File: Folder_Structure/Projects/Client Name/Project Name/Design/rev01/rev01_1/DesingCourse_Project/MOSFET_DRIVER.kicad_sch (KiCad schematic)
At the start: 42 parts, among them U2 DRV8302DCA

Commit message: Update 6
SCH and LIB for MOSFET page done, missing passive components
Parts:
- removed L1: 22u, symbol Device:L
- added L?: 22u, IND_BOURNS_SDR0805, symbol SDR0805-220ML:SDR0805-220ML
- D4: MPN (none) -> PMEG6020AELR; Manufactuere (none) -> Nexperia
- D5: MPN (none) -> BAT60A; Manufacturer (none) -> Inineon
- U2: MPN (none) -> DRV8302DCA; Manufacturer (none) -> Texas Instruments
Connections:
- net P5V_DRV: now also L?.2
- net PH: now also L?.1
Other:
- note added: "MOSFET DRIVER"
- note removed: "MOSFER DRIVER"
- company: (none) -> Integro Consulting AB
- title: (none) -> PCB Mastery Project

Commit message: Update 11
SCH finishe, missing the labels and logos and adding all passive components
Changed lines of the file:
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@@
 	(text "MOSFET DRIVER\n"
 		(exclude_from_sim no)
-		(at 144.78 20.066 0)
+		(at 160.02 20.32 0)
 		(effects
 			(font

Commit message: Update 12
Until STEP-DOWN page, all components have complete libraries.

Creation and incluison of all logos and labels libraries
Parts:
- removed C22, C23, C24, C25, C26, C27: 1u, symbol Device:C
- removed R18, R20, R22: 39k, symbol Device:R
- added C36, C37, C38, C40, C41, C43: 1u, Capacitor_SMD:C_0603_1608Metric, symbol Device:C
- added R27, R29, R31: 39k, Resistor_SMD:R_0603_1608Metric, symbol Device:R
- C35: value 1u -> 100n
- gave numbers to parts that had none: 1
- renumbered C33 to C24, C31 to C25, C29 to C26, C34 to C27, C32 to C28, C30 to C29, C28 to C30, C21 to C31, C18 to C32, C19 to C33, C20 to C34, C36 to C39, C37 to C42, C38 to C44, C39 to C45, C40 to C46, C41 to C47, D4 to D13, D5 to D14, R12 to R20, R13 to R21, R14 to R22, R11 to R23, R15 to R24, R16 to R25, R17 to R26, R23 to R28, R21 to R30, R19 to R32, U2 to U4
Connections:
- net +VDC: now also C36.1, C37.1, C38.1, C40.1, C41.1, C43.1
- net GND: now also C36.2, C37.2, C38.2, C40.2, C41.2, C43.2
- net H1_VS: now also R31.1
- net H2_VS: now also R29.1
- net H3_VS: now also R27.1
- net SENS1: now also R31.2
- net SENS2: now also R29.2
- net SENS3: now also R27.2

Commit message: Update13
Still working on FP for the MCU
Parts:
- C32, C33, C34, C35, C45, C46, C47: footprint (none) -> Capacitor_SMD:C_0603_1608Metric; Package (none) -> 0603; Temp Coeff (none) -> X7R; Tolerance (none) -> 10%; Voltage Rating (none) -> 10V
- C39, C42, C44: footprint (none) -> Capacitor_SMD:C_0603_1608Metric; Package (none) -> 0603; Temp Coeff (none) -> X5R; Tolerance (none) -> 10%; Voltage Rating (none) -> 10V
- R28, R30, R32: footprint (none) -> Resistor_SMD:R_0603_1608Metric; Package (none) -> 0603; Power Rating (none) -> 1/10W; Tolerance (none) -> 1%

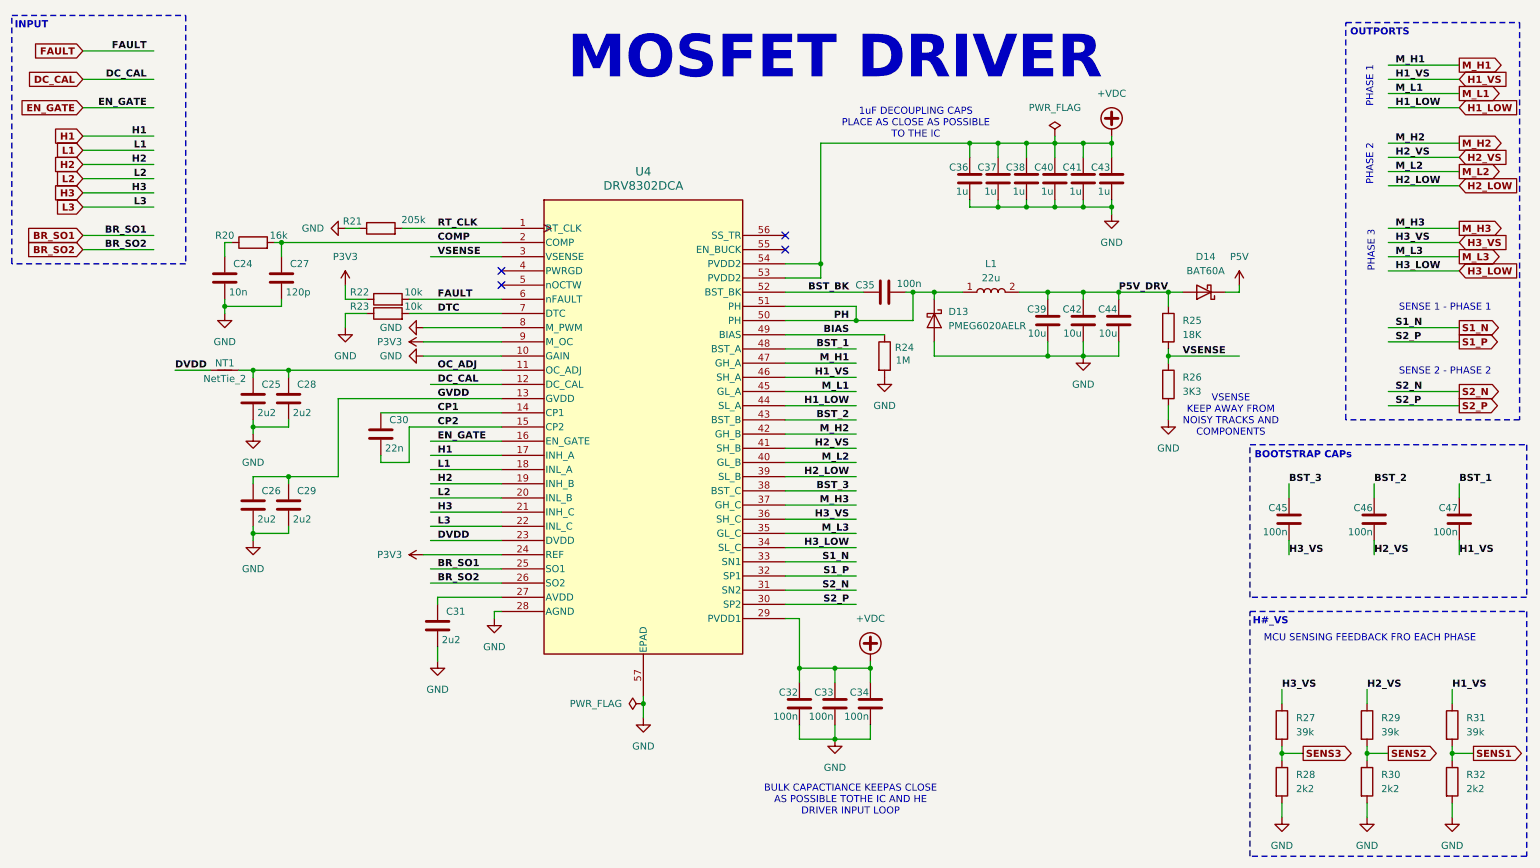
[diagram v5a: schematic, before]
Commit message: Update14
All components with FP, missing the block diagram
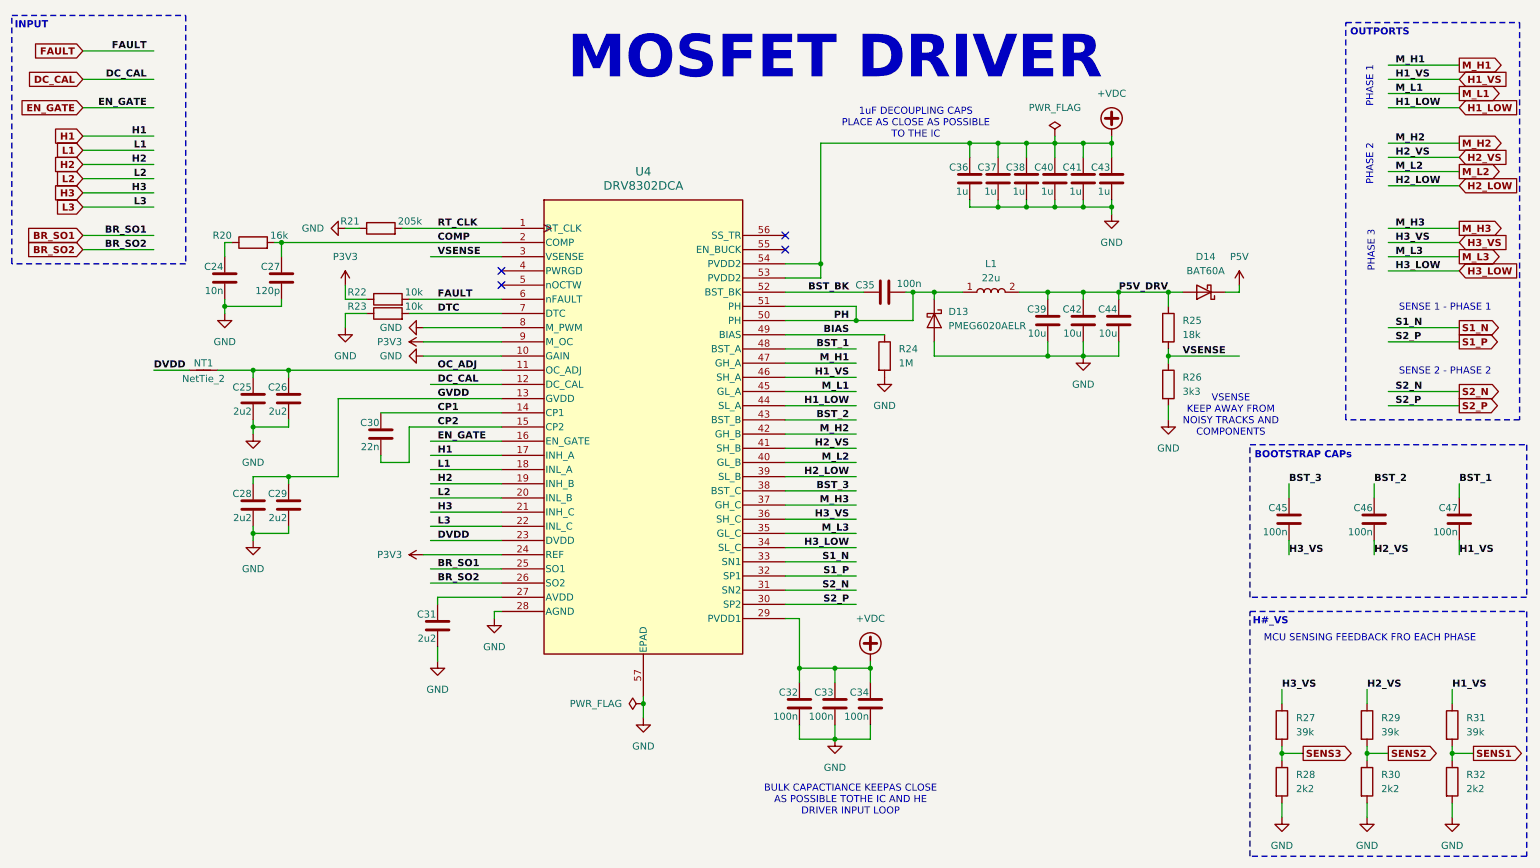
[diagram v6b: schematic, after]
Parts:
- C24, C27: footprint (none) -> Capacitor_SMD:C_0603_1608Metric; Package (none) -> 0603; Temp Coeff (none) -> X7R; Tolerance (none) -> 10%; Voltage Rating (none) -> 50V
- C25, C26, C28, C29, C31: footprint (none) -> Capacitor_SMD:C_0603_1608Metric; Package (none) -> 0603; Temp Coeff (none) -> X5R; Tolerance (none) -> 10%; Voltage Rating (none) -> 6.3V
- C30: footprint (none) -> Capacitor_SMD:C_0603_1608Metric; Package (none) -> 0603; Temp Coeff (none) -> X7R; Tolerance (none) -> 10%; Voltage Rating (none) -> 100V
- D13: Manufactuere Nexperia -> (none); Manufacturer (none) -> Nexperia; Package (none) -> SOD-123
- D14: Manufacturer Inineon -> Infineon; Package (none) -> SOD-323
- NT1: footprint (none) -> NetTie:NetTie-2_SMD_Pad0.5mm
- R20, R21, R22, R23, R24: footprint (none) -> Resistor_SMD:R_0603_1608Metric; Package (none) -> 0603; Power Rating (none) -> 1/10W; Tolerance (none) -> 1%
- R25: value 18K -> 18k; footprint (none) -> Resistor_SMD:R_0603_1608Metric; Package (none) -> 0603; Power Rating (none) -> 1/10W; Tolerance (none) -> 1%
- R26: value 3K3 -> 3k3; footprint (none) -> Resistor_SMD:R_0603_1608Metric; Package (none) -> 0603; Power Rating (none) -> 1/10W; Tolerance (none) -> 1%
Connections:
- net GVDD: now also C28.1; no longer C26.1
- net OC_ADJ: now also C26.1; no longer C28.1
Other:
- moved on the sheet: NT1

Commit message: Update 16
Initial component placement done
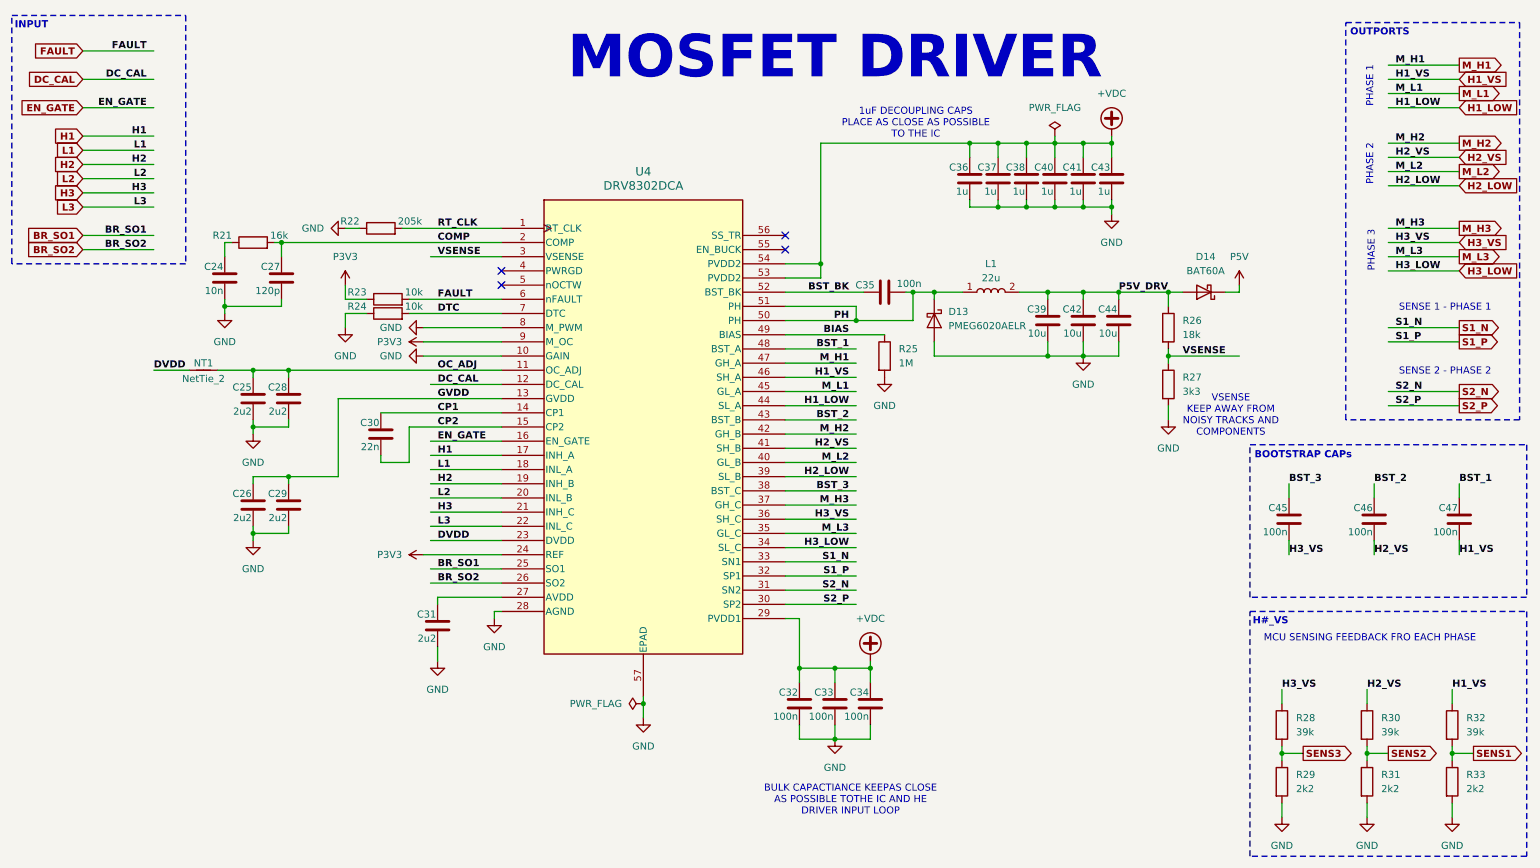
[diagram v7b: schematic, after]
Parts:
- L1: footprint IND_BOURNS_SDR0805 -> L_Bourns_SDR0805:IND_BOURNS_SDR0805
- U4: footprint DCA56_6P35X3P61 -> DRV8302DCA:SOP50P810X120-57N; Package (none) -> 56pin-HTSSOP
- renumbered C28 to C26, C26 to C28, R20 to R21, R21 to R22, R22 to R23, R23 to R24, R24 to R25, R25 to R26, R26 to R27, R27 to R28, R28 to R29, R29 to R30, R30 to R31, R31 to R32, R32 to R33
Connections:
- net S1_P: no longer U4.30 (SP2)
- new net S2_P: U4.30 (SP2)

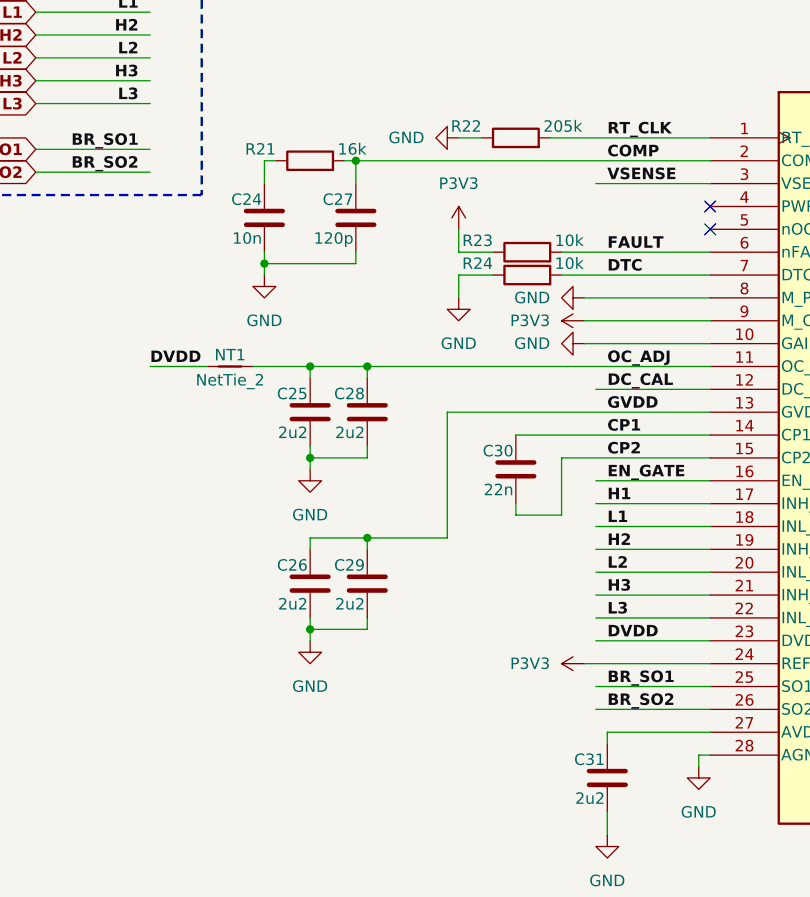
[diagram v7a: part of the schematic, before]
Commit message: Update17
Design rules and stack defined.

Check againg DR and proceed with layout.
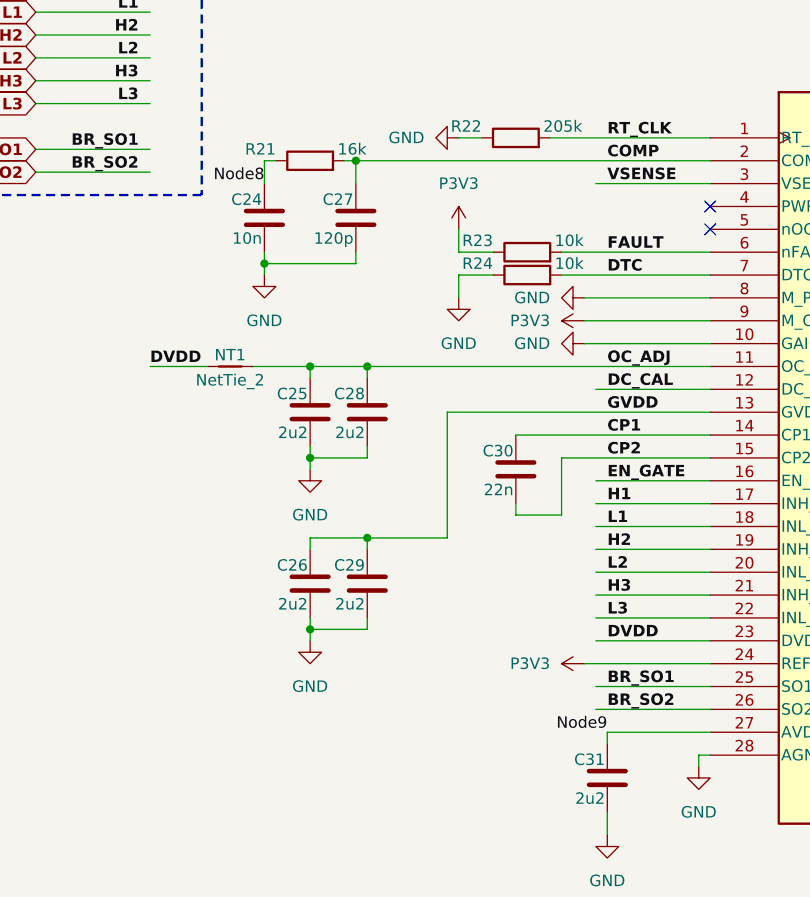
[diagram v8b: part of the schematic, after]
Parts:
- C39, C42, C44: footprint Capacitor_SMD:C_0603_1608Metric -> Capacitor_SMD:C_1210_3225Metric; Package 0603 -> 1210; Voltage Rating 10V -> 16V
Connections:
- net Node8: now reaches C24.1, R21.1
- net at C31.1, U4.27 (AVDD): no longer names the net of C31.1, U4.27 (AVDD)
